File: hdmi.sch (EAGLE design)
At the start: 143 parts, among them IC1 FT2232HQ, U0 6SLX45CSG324, U1 MT41J64M16, U2 TPD12S016RKTR, U3 TPD12S016RKTR, U4 TPD12S016RKTR, U5 MNR18, U6 MNR18, U8 20Mhz

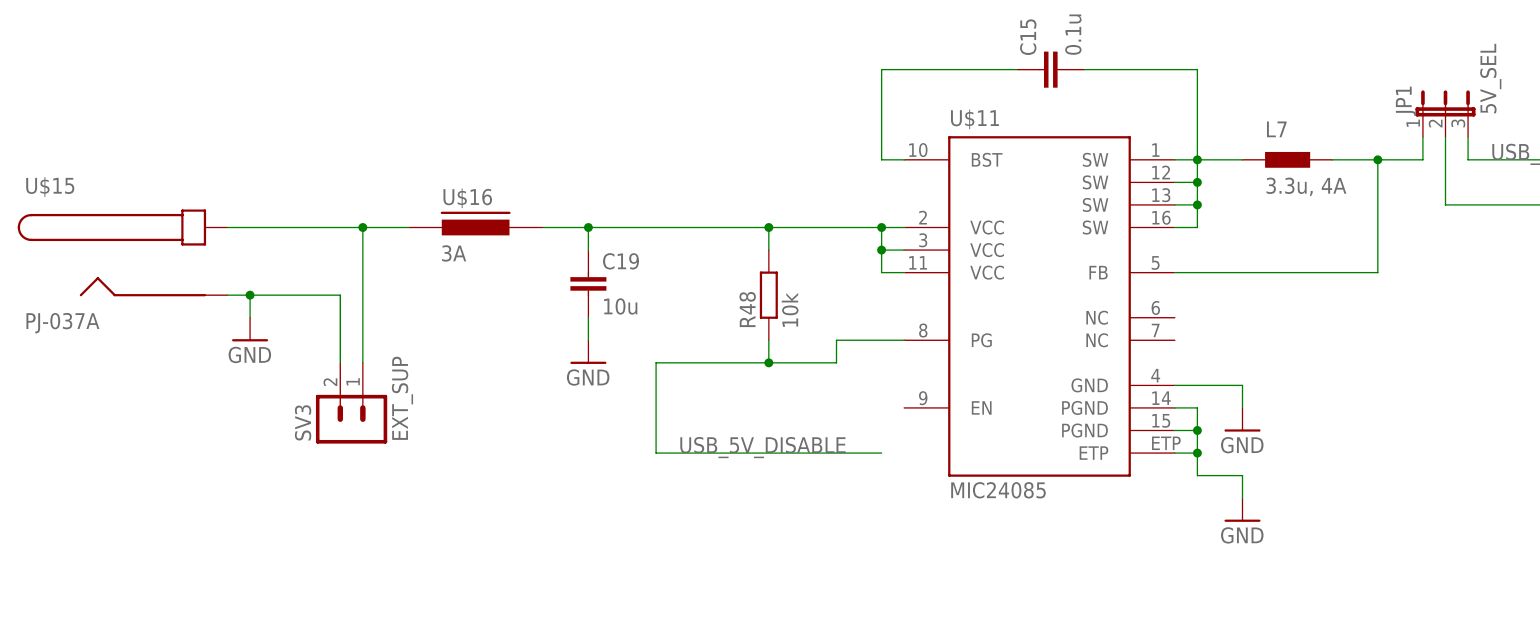
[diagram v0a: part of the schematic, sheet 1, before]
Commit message: +Toslink
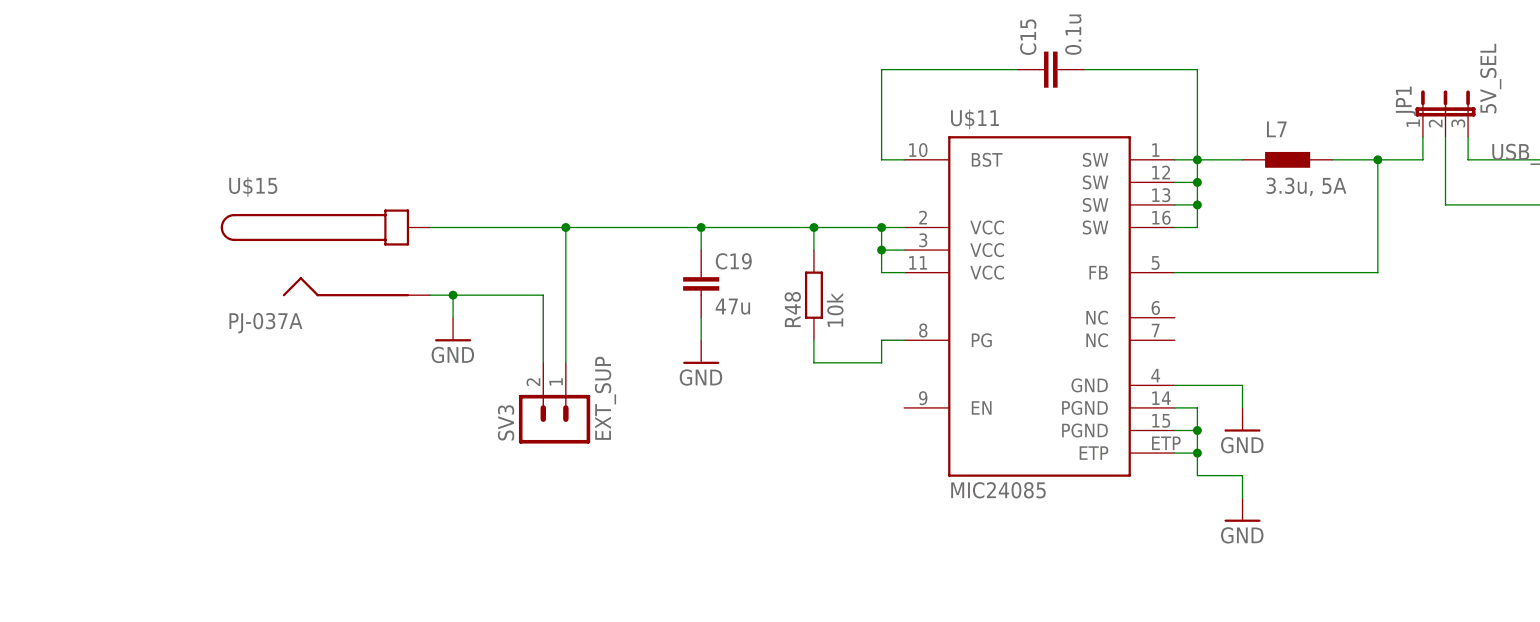
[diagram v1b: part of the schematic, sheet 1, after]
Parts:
- removed U$16: 3A, prj-hdmi:FERRITE0603
- added C23, C62, C63: 0.1u, prj-hdmi:C-EU0402
- added L8, L9: 47u, prj-hdmi:INDUCTOR0603
- added U$14: PLT133-T10W, prj-hdmi:PLT133-T10W
- added U$17, U$18: PLR135-T10, prj-hdmi:PLR135-T10
- C19: value 10u -> 47u; device prj-hdmi:C-EU0603 -> prj-hdmi:C-EU0805
- C7: value 10u -> 47u; device prj-hdmi:C-EU0402 -> prj-hdmi:C-EU0805
- L7: value 3.3u, 4A -> 3.3u, 5A; device prj-hdmi:INDUCTOR1008 -> prj-hdmi:INDUCTORSRTP5030T
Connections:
- removed net N$29: C19.1, R48.2, U$11.VCC@11, U$11.VCC@2, U$11.VCC@3, U$16.2
- new net N$36: C23.1, L8.2, U$18.VCC
- new net N$4: C62.1, L9.2, U$17.VCC
- new net TOS_IN0: U$18.VOUT
- new net TOS_IN1: U$17.VOUT
- new net TOS_OUT0: U$14.VIN
- net +3V3: now also C57.1, C63.1, L8.1, L9.1, U$14.VCC; no longer C57.2
- net CENTER: now also C19.1, R48.2, U$11.VCC@11, U$11.VCC@2, U$11.VCC@3; no longer U$16.1
- net GND: now also C23.2, C57.2, C62.2, C63.2, U$14.GND, U$17.GND, U$18.GND; no longer C57.1
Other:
- moved on the sheet: C17, C18, C19, C20, C57, R48, SV3, U$15

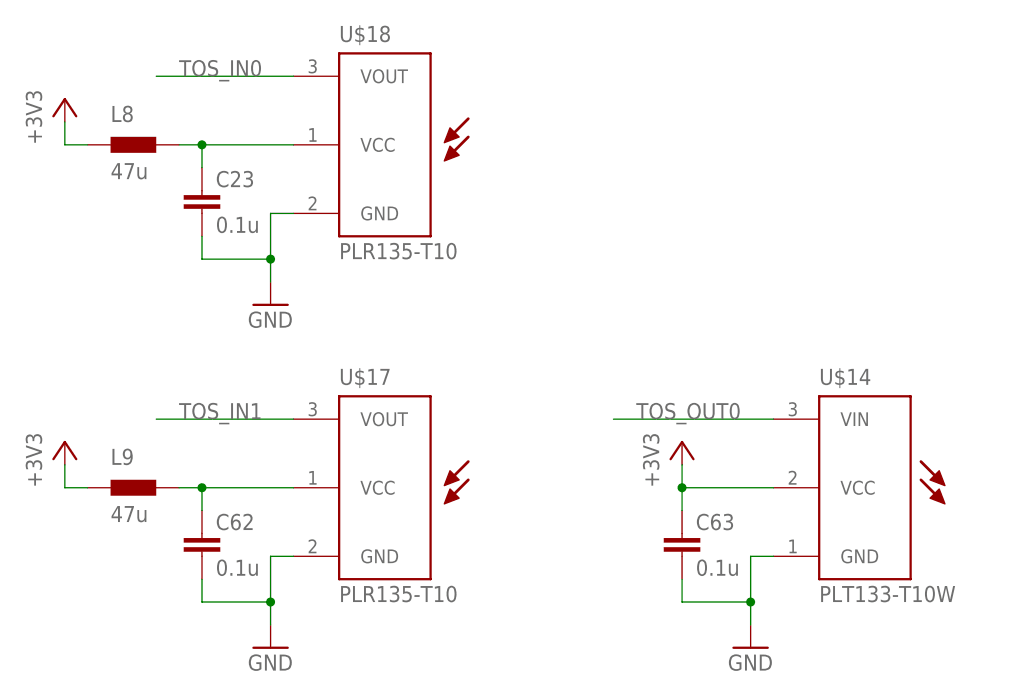
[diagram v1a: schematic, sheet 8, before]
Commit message: +Toslink connections
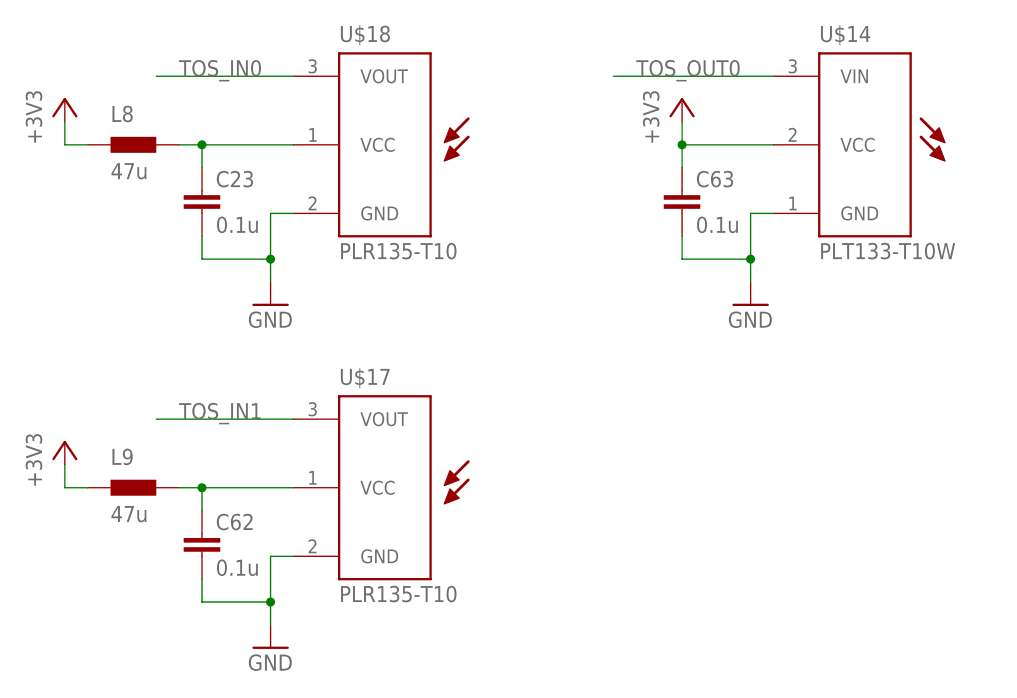
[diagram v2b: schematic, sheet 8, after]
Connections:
- new net N$19: R48.1, U$11.PG
- net TOS_IN0: now also U0B0.IO_L2N_0
- net TOS_IN1: now also U0B1.IO_L51N_M1DQ13_1
- net TOS_OUT0: now also U0B2.IO_L45N_2
- net USB_5V_DISABLE: no longer R48.1, U$11.PG
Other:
- moved on the sheet: C63, U$14
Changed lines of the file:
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@@
 </segment>
 </net>
-<net name="USB_5V_DISABLE" class="0">
+<net name="N$19" class="0">
 <segment>
 <pinref part="U$11" gate="G$1" pin="PG"/>
 <wire x1="96.52" y1="129.54" x2="93.98" y2="129.54" width="0.1524" layer="91"/>
 <wire x1="93.98" y1="129.54" x2="93.98" y2="127" width="0.1524" layer="91"/>
-<wire x1="93.98" y1="127" x2="86.36" y2="127" width="0.1524" layer="91"/>
 <pinref part="R48" gate="G$1" pin="1"/>
+<wire x1="93.98" y1="127" x2="86.36" y2="127" width="0.1524" layer="91"/>
 <wire x1="86.36" y1="127" x2="86.36" y2="129.54" width="0.1524" layer="91"/>
 </segment>
@@
 </segment>
 </net>
+<net name="TOS_IN0" class="0">
+<segment>
+<pinref part="U0" gate="B0" pin="IO_L2N_0"/>
+<wire x1="27.94" y1="119.38" x2="48.26" y2="119.38" width="0.1524" layer="91"/>
+<label x="30.48" y="119.38" size="1.778" layer="95"/>
+</segment>
+</net>
 </nets>
 </sheet>
@@
 </segment>
 </net>
+<net name="TOS_IN1" class="0">
+<segment>
+<pinref part="U0" gate="B1" pin="IO_L51N_M1DQ13_1"/>
+<wire x1="27.94" y1="33.02" x2="48.26" y2="33.02" width="0.1524" layer="91"/>
+<label x="30.48" y="33.02" size="1.778" layer="95"/>
+</segment>
+</net>
 </nets>
 </sheet>
@@
 </segment>
 </net>
+<net name="TOS_OUT0" class="0">
+<segment>
+<pinref part="U0" gate="B2" pin="IO_L45N_2"/>
+<wire x1="30.48" y1="53.34" x2="50.8" y2="53.34" width="0.1524" layer="91"/>
+<label x="33.02" y="53.34" size="1.778" layer="95"/>
+</segment>
+</net>
 </nets>
 </sheet>
@@
 </plain>
 <instances>
-<instance part="U$14" gate="G$1" x="101.6" y="25.4"/>
+<instance part="U$14" gate="G$1" x="101.6" y="63.5"/>
 <instance part="U$17" gate="G$1" x="48.26" y="25.4"/>
 <instance part="U$18" gate="G$1" x="48.26" y="63.5"/>
 <instance part="GND61" gate="1" x="35.56" y="7.62"/>
 <instance part="GND62" gate="1" x="35.56" y="45.72"/>
-<instance part="GND63" gate="1" x="88.9" y="7.62"/>
+<instance part="GND63" gate="1" x="88.9" y="45.72"/>
 <instance part="+3V16" gate="G$1" x="12.7" y="68.58"/>
-<instance part="+3V17" gate="G$1" x="81.28" y="30.48"/>
+<instance part="+3V17" gate="G$1" x="81.28" y="68.58"/>
 <instance part="+3V18" gate="G$1" x="12.7" y="30.48"/>
 <instance part="C23" gate="G$1" x="27.94" y="58.42"/>
 <instance part="C62" gate="G$1" x="27.94" y="20.32"/>
-<instance part="C63" gate="G$1" x="81.28" y="20.32"/>
+<instance part="C63" gate="G$1" x="81.28" y="58.42"/>
 <instance part="L8" gate="G$1" x="20.32" y="63.5"/>
 <instance part="L9" gate="G$1" x="20.32" y="25.4"/>
@@
 <segment>
 <pinref part="GND63" gate="1" pin="GND"/>
-<wire x1="88.9" y1="10.16" x2="88.9" y2="12.7" width="0.1524" layer="91"/>
+<wire x1="88.9" y1="48.26" x2="88.9" y2="50.8" width="0.1524" layer="91"/>
 <pinref part="U$14" gate="G$1" pin="GND"/>
-<wire x1="88.9" y1="12.7" x2="88.9" y2="17.78" width="0.1524" layer="91"/>
-<wire x1="88.9" y1="17.78" x2="91.44" y2="17.78" width="0.1524" layer="91"/>
+<wire x1="88.9" y1="50.8" x2="88.9" y2="55.88" width="0.1524" layer="91"/>
+<wire x1="88.9" y1="55.88" x2="91.44" y2="55.88" width="0.1524" layer="91"/>
 <pinref part="C63" gate="G$1" pin="2"/>
-<wire x1="88.9" y1="12.7" x2="81.28" y2="12.7" width="0.1524" layer="91"/>
-<wire x1="81.28" y1="12.7" x2="81.28" y2="15.24" width="0.1524" layer="91"/>
-<junction x="88.9" y="12.7"/>
+<wire x1="88.9" y1="50.8" x2="81.28" y2="50.8" width="0.1524" layer="91"/>
+<wire x1="81.28" y1="50.8" x2="81.28" y2="53.34" width="0.1524" layer="91"/>
+<junction x="88.9" y="50.8"/>
 </segment>
 <segment>
@@
 <pinref part="U$14" gate="G$1" pin="VCC"/>
 <pinref part="+3V17" gate="G$1" pin="+3V3"/>
-<wire x1="91.44" y1="25.4" x2="81.28" y2="25.4" width="0.1524" layer="91"/>
-<wire x1="81.28" y1="25.4" x2="81.28" y2="27.94" width="0.1524" layer="91"/>
+<wire x1="91.44" y1="63.5" x2="81.28" y2="63.5" width="0.1524" layer="91"/>
+<wire x1="81.28" y1="63.5" x2="81.28" y2="66.04" width="0.1524" layer="91"/>
 <pinref part="C63" gate="G$1" pin="1"/>
-<wire x1="81.28" y1="22.86" x2="81.28" y2="25.4" width="0.1524" layer="91"/>
-<junction x="81.28" y="25.4"/>
+<wire x1="81.28" y1="60.96" x2="81.28" y2="63.5" width="0.1524" layer="91"/>
+<junction x="81.28" y="63.5"/>
 </segment>
 <segment>
@@
 <segment>
 <pinref part="U$14" gate="G$1" pin="VIN"/>
-<wire x1="91.44" y1="33.02" x2="73.66" y2="33.02" width="0.1524" layer="91"/>
-<label x="76.2" y="33.02" size="1.778" layer="95"/>
+<wire x1="91.44" y1="71.12" x2="73.66" y2="71.12" width="0.1524" layer="91"/>
+<label x="76.2" y="71.12" size="1.778" layer="95"/>
 </segment>
 </net>

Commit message: +Schematic notes
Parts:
- removed R48: 10k, prj-hdmi:R-EU_0402
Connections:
- removed net N$19: R48.1, U$11.PG
- net CENTER: no longer R48.2
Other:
- note added: "5V, 3A max."
- note added: "6-18V, 15 Watt max."
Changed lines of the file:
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@@
 <part name="GND47" library="supply1" deviceset="GND" device=""/>
 <part name="GND59" library="supply1" deviceset="GND" device=""/>
-<part name="R48" library="prj-hdmi" deviceset="R-EU_" device="0402" value="10k"/>
 <part name="GND53" library="supply1" deviceset="GND" device=""/>
 <part name="SV3" library="prj-hdmi" deviceset="MA02-1" device="" value="EXT_SUP"/>
@@
 <description>Power</description>
 <plain>
+<text x="48.26" y="144.78" size="2.54" layer="97">6-18V, 15 Watt max.</text>
+<text x="132.08" y="139.7" size="2.54" layer="97">5V, 3A max.</text>
 </plain>
 <instances>
@@
 <instance part="GND47" gate="1" x="134.62" y="109.22"/>
 <instance part="GND59" gate="1" x="134.62" y="119.38"/>
-<instance part="R48" gate="G$1" x="86.36" y="134.62" rot="R90"/>
 <instance part="GND53" gate="1" x="73.66" y="127"/>
 <instance part="SV3" gate="G$1" x="55.88" y="119.38" rot="R90"/>
@@
 <pinref part="U$11" gate="G$1" pin="VCC@2"/>
 <pinref part="U$11" gate="G$1" pin="VCC@3"/>
-<wire x1="73.66" y1="142.24" x2="86.36" y2="142.24" width="0.1524" layer="91"/>
-<wire x1="86.36" y1="142.24" x2="93.98" y2="142.24" width="0.1524" layer="91"/>
+<wire x1="73.66" y1="142.24" x2="93.98" y2="142.24" width="0.1524" layer="91"/>
 <wire x1="93.98" y1="142.24" x2="96.52" y2="142.24" width="0.1524" layer="91"/>
 <wire x1="96.52" y1="139.7" x2="93.98" y2="139.7" width="0.1524" layer="91"/>
@@
 <wire x1="93.98" y1="137.16" x2="93.98" y2="139.7" width="0.1524" layer="91"/>
 <junction x="93.98" y="139.7"/>
-<pinref part="R48" gate="G$1" pin="2"/>
-<wire x1="86.36" y1="139.7" x2="86.36" y2="142.24" width="0.1524" layer="91"/>
-<junction x="86.36" y="142.24"/>
 <pinref part="C19" gate="G$1" pin="1"/>
 <wire x1="73.66" y1="139.7" x2="73.66" y2="142.24" width="0.1524" layer="91"/>
@@
 </segment>
 </net>
-<net name="SW@16" class="0">
+<net name="SW@16" class="1">
 <segment>
 <pinref part="C15" gate="G$1" pin="2"/>
@@
 </segment>
 </net>
-<net name="N$30" class="0">
+<net name="N$30" class="1">
 <segment>
 <pinref part="JP1" gate="1" pin="1"/>
-<wire x1="149.86" y1="149.86" x2="154.94" y2="149.86" width="0.1524" layer="91"/>
+<wire x1="152.4" y1="149.86" x2="154.94" y2="149.86" width="0.1524" layer="91"/>
 <wire x1="154.94" y1="149.86" x2="154.94" y2="152.4" width="0.1524" layer="91"/>
-<wire x1="149.86" y1="137.16" x2="149.86" y2="149.86" width="0.1524" layer="91"/>
+<wire x1="152.4" y1="137.16" x2="152.4" y2="149.86" width="0.1524" layer="91"/>
 <pinref part="U$11" gate="G$1" pin="FB"/>
-<wire x1="149.86" y1="137.16" x2="127" y2="137.16" width="0.1524" layer="91"/>
+<wire x1="152.4" y1="137.16" x2="127" y2="137.16" width="0.1524" layer="91"/>
 <pinref part="L7" gate="G$1" pin="2"/>
-<wire x1="149.86" y1="149.86" x2="144.78" y2="149.86" width="0.1524" layer="91"/>
-<junction x="149.86" y="149.86"/>
-</segment>
-</net>
-<net name="N$19" class="0">
-<segment>
-<pinref part="U$11" gate="G$1" pin="PG"/>
-<wire x1="96.52" y1="129.54" x2="93.98" y2="129.54" width="0.1524" layer="91"/>
-<wire x1="93.98" y1="129.54" x2="93.98" y2="127" width="0.1524" layer="91"/>
-<pinref part="R48" gate="G$1" pin="1"/>
-<wire x1="93.98" y1="127" x2="86.36" y2="127" width="0.1524" layer="91"/>
-<wire x1="86.36" y1="127" x2="86.36" y2="129.54" width="0.1524" layer="91"/>
-</segment>
-</net>
+<wire x1="152.4" y1="149.86" x2="144.78" y2="149.86" width="0.1524" layer="91"/>
+<junction x="152.4" y="149.86"/>
+</segment>
+</net>

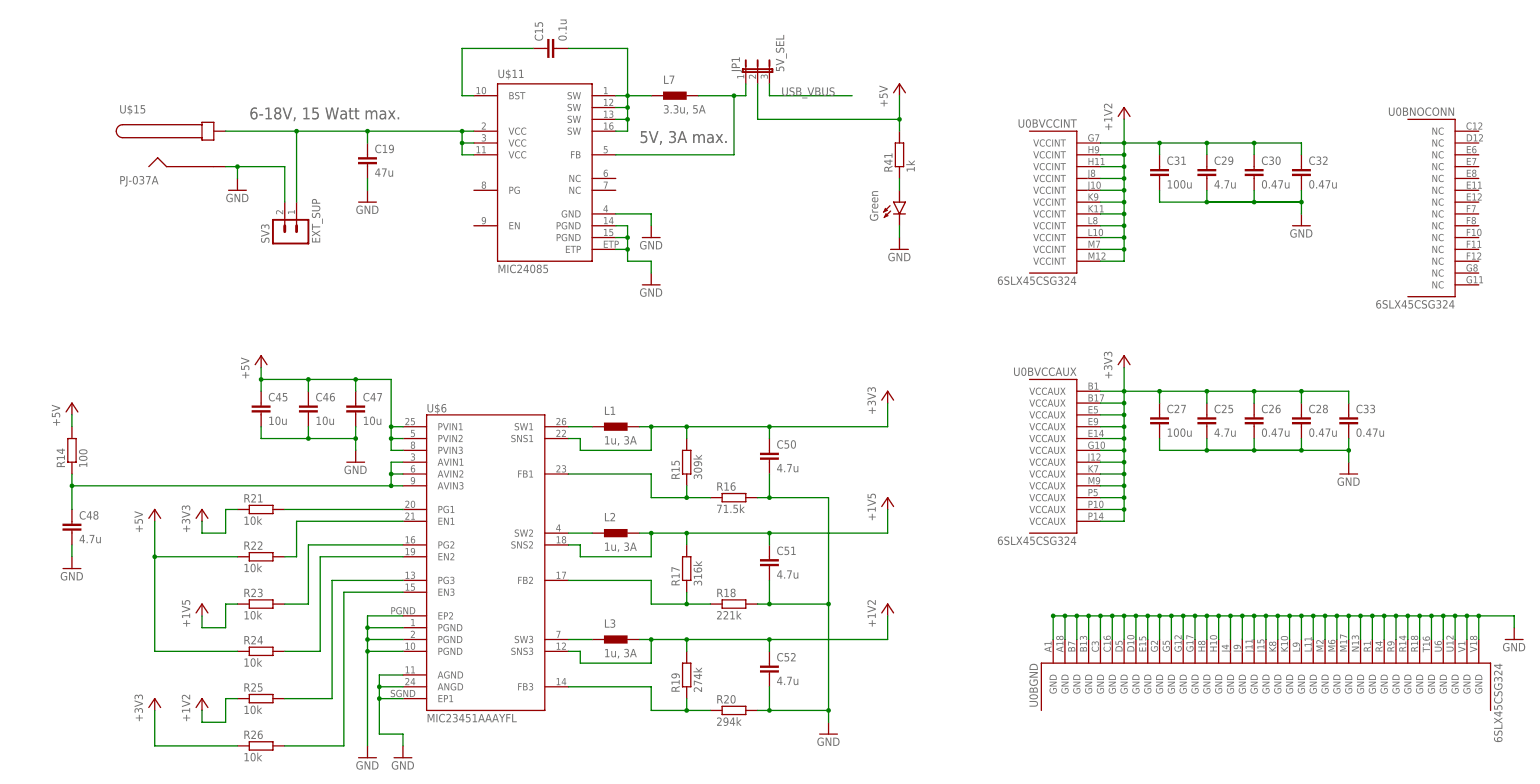
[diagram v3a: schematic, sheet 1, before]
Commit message: Removed regulator for external power, schematics look good I think
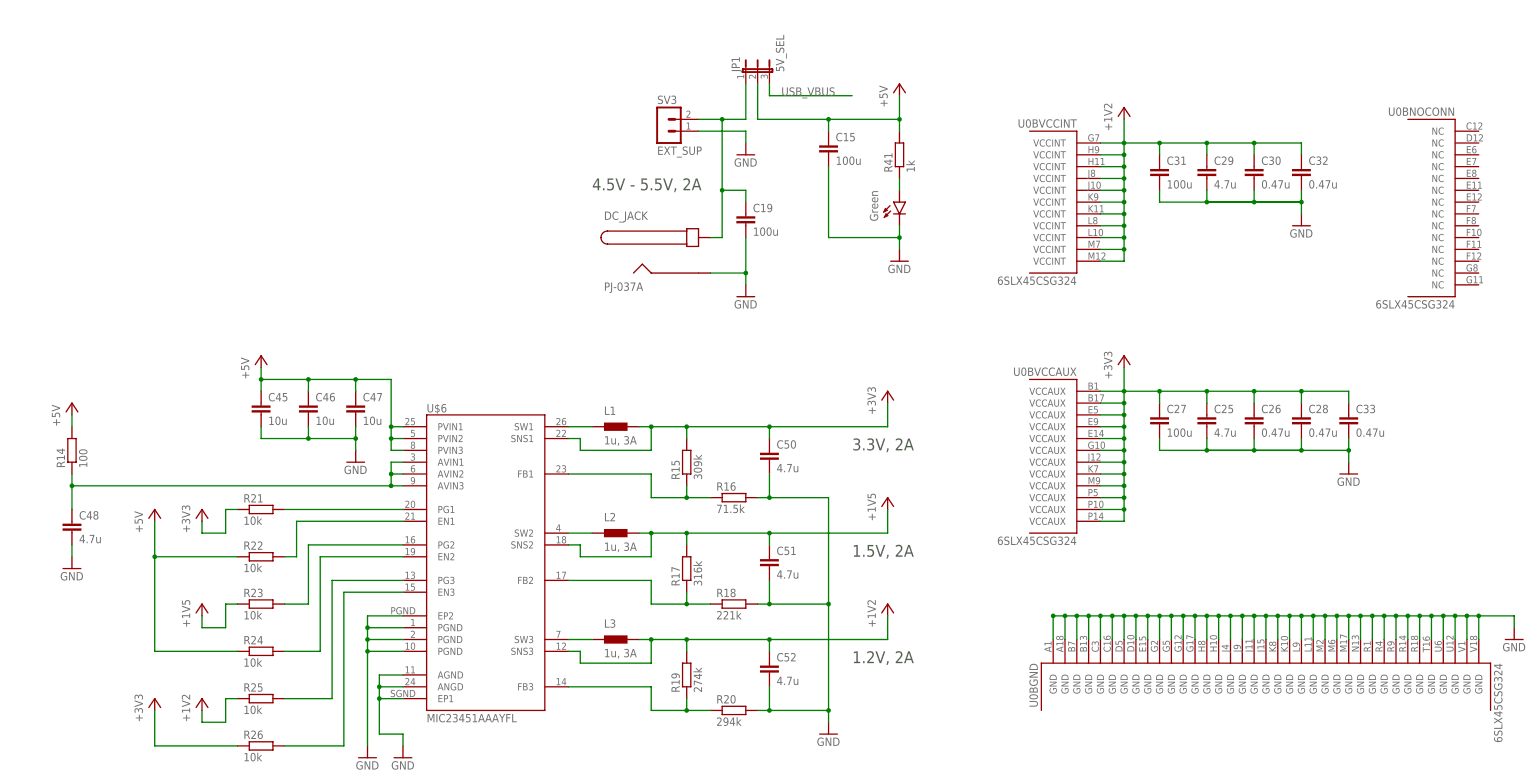
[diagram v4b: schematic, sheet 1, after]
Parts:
- removed L6: 1A, prj-hdmi:FERRITE0603
- removed L7: 3.3u, 5A, prj-hdmi:INDUCTORSRTP5030T
- removed U$11: MIC24085, prj-hdmi:MIC24085
- removed U$15: PJ-037A, prj-hdmi:PJ-037A
- added DC_JACK: PJ-037A, prj-hdmi:PJ-037A
- C15: value 0.1u -> 100u; device prj-hdmi:C-EU0603 -> rcl:C-EUC1206
- C19: value 47u -> 100u; device prj-hdmi:C-EU0805 -> rcl:C-EUC1206
- C7: value 47u -> 100u
- renumbered U$14 to TOSLINK_OUT0, U$17 to TOSLINK_IN1, U$18 to TOSLINK_IN0
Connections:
- removed net N$2: C15.1, U$11.BST
- removed net N$30: JP1.1, L7.2, U$11.FB
- removed net N$48: C7.1, L6.2, U$10.VBUS@10, U$10.VBUS@9
- removed net SW@16: C15.2, L7.1, U$11.SW@1, U$11.SW@12, U$11.SW@13, U$11.SW@16
- net +5V: now also C15.1
- net CENTER: now also DC_JACK.CENTER, JP1.1, SV3.2; no longer SV3.1, U$11.VCC@11, U$11.VCC@2, U$11.VCC@3, U$15.CENTER
- net GND: now also C15.2, DC_JACK.BARREL, SV3.1; no longer SV3.2, U$11.ETP, U$11.GND, U$11.PGND@14, U$11.PGND@15, U$15.BARREL
- net N$45: now also C7.1, U$10.VBUS@10, U$10.VBUS@9; no longer L6.1
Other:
- note added: "1.2V, 2A"
- note added: "1.5V, 2A"
- note added: "3.3V, 2A"
- note added: "4.5V - 5.5V, 2A"
- note removed: "5V, 3A max."
- note removed: "6-18V, 15 Watt max."
- moved on the sheet: C15, C19, C7, SV3
